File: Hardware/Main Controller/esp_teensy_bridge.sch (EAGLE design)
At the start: 9 parts, among them IC1 BQ79600PWRQ1

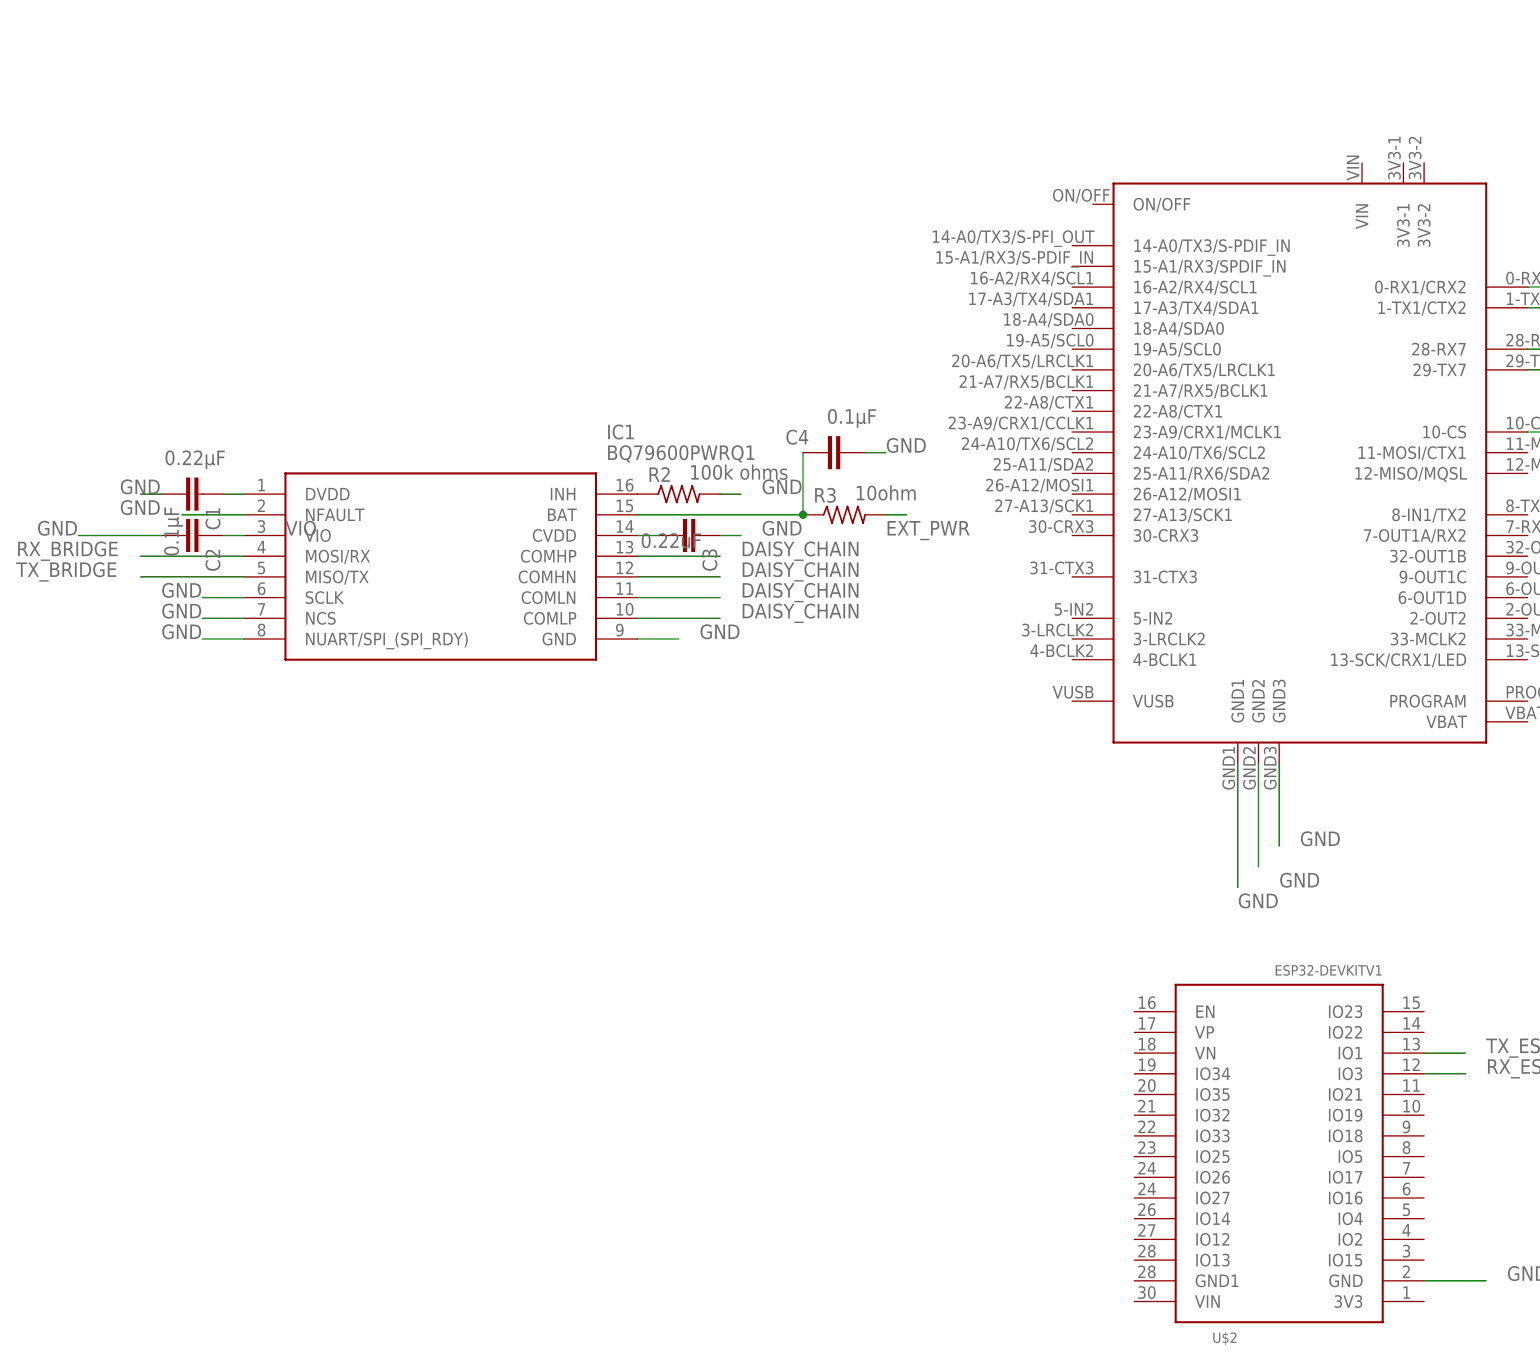
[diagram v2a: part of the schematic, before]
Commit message: Update esp_teensy_bridge.sch
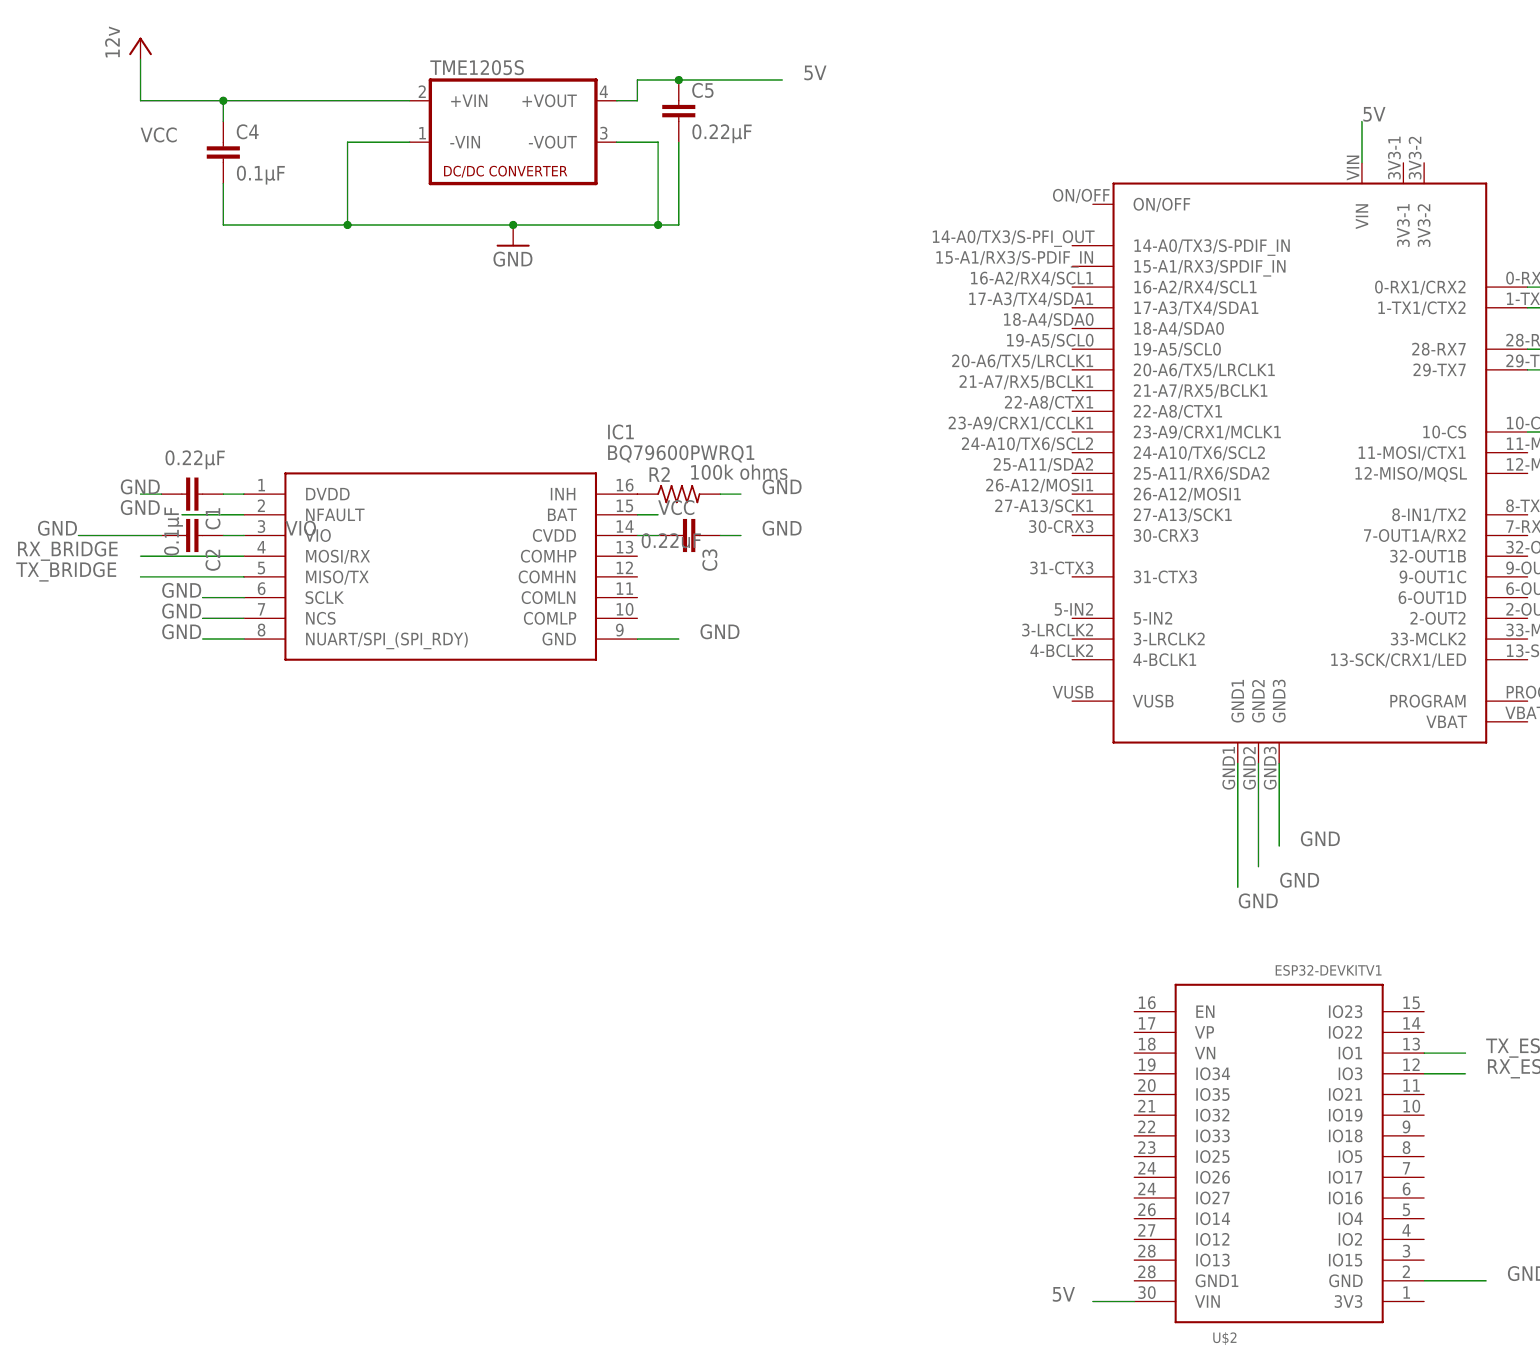
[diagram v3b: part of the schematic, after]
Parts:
- removed R3: 10ohm, rcl:R-US_0204/7
- added C5: 0.22μF, capacitor-wima:C2,5-3
- added TME1205S: (no value), dc-dc-converter:NME
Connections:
- removed net DAISY_CHAIN: IC1.COMHN, IC1.COMHP, IC1.COMLN, IC1.COMLP
- removed net EXT_PWR: R3.2
- removed net N$5: C4.2, IC1.BAT, R3.1
- new net 5V: C5.1, TME1205S.+VOUT, U$1.VIN, U$2.VIN
- new net VCC: C4.1, IC1.BAT, TME1205S.+VIN
- net GND: now also C4.2, C5.2, TME1205S.-VIN, TME1205S.-VOUT; no longer C4.1
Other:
- moved on the sheet: C4
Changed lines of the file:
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@@
 <part name="C3" library="capacitor-wima" library_urn="urn:adsk.eagle:library:116" deviceset="C" device="2.5/2" package3d_urn="urn:adsk.eagle:package:5415/1" value="0.22uF"/>
 <part name="R2" library="rcl" library_urn="urn:adsk.eagle:library:334" deviceset="R-US_" device="0204/7" package3d_urn="urn:adsk.eagle:package:23498/2" value="100k ohms"/>
-<part name="R3" library="rcl" library_urn="urn:adsk.eagle:library:334" deviceset="R-US_" device="0204/7" package3d_urn="urn:adsk.eagle:package:23498/2" value="10ohm"/>
+<part name="TME1205S" library="dc-dc-converter" library_urn="urn:adsk.eagle:library:208" deviceset="NME" device="" package3d_urn="urn:adsk.eagle:package:12313/1"/>
+<part name="GND1" library="supply1" library_urn="urn:adsk.eagle:library:371" deviceset="GND" device=""/>
+<part name="C5" library="capacitor-wima" library_urn="urn:adsk.eagle:library:116" deviceset="C" device="2,5-3" package3d_urn="urn:adsk.eagle:package:5436/1" value="0.22μF"/>
+<part name="P+1" library="supply1" library_urn="urn:adsk.eagle:library:371" deviceset="VCC" device="" value="12v"/>
 <part name="C4" library="capacitor-wima" library_urn="urn:adsk.eagle:library:116" deviceset="C" device="2,5-3" package3d_urn="urn:adsk.eagle:package:5436/1" value="0.1μF"/>
 </parts>
@@
 <attribute name="VALUE" x="-8.89" y="67.818" size="1.778" layer="96"/>
 </instance>
-<instance part="R3" gate="G$1" x="10.16" y="63.5" smashed="yes">
-<attribute name="NAME" x="6.35" y="64.9986" size="1.778" layer="95"/>
-<attribute name="VALUE" x="11.43" y="65.278" size="1.778" layer="96"/>
-</instance>
-<instance part="C4" gate="G$1" x="10.16" y="71.12" smashed="yes" rot="R270">
-<attribute name="NAME" x="2.921" y="72.136" size="1.778" layer="95"/>
-<attribute name="VALUE" x="8.001" y="74.676" size="1.778" layer="96"/>
+<instance part="TME1205S" gate="G$1" x="-30.48" y="111.76" smashed="yes">
+<attribute name="NAME" x="-40.64" y="117.475" size="1.778" layer="95"/>
+<attribute name="VALUE" x="-40.64" y="101.6" size="1.778" layer="96"/>
+</instance>
+<instance part="GND1" gate="1" x="-30.48" y="96.52" smashed="yes">
+<attribute name="VALUE" x="-33.02" y="93.98" size="1.778" layer="96"/>
+</instance>
+<instance part="C5" gate="G$1" x="-10.16" y="114.3" smashed="yes">
+<attribute name="NAME" x="-8.636" y="114.681" size="1.778" layer="95"/>
+<attribute name="VALUE" x="-8.636" y="109.601" size="1.778" layer="96"/>
+</instance>
+<instance part="P+1" gate="VCC" x="-76.2" y="121.92" smashed="yes">
+<attribute name="VALUE" x="-78.74" y="119.38" size="1.778" layer="96" rot="R90"/>
+</instance>
+<instance part="C4" gate="G$1" x="-66.04" y="109.22" smashed="yes">
+<attribute name="NAME" x="-64.516" y="109.601" size="1.778" layer="95"/>
+<attribute name="VALUE" x="-64.516" y="104.521" size="1.778" layer="96"/>
 </instance>
 </instances>
@@
 </busses>
 <nets>
-<net name="DAISY_CHAIN" class="0">
-<segment>
-<pinref part="IC1" gate="G$1" pin="COMHP"/>
-<wire x1="-15.24" y1="58.42" x2="-5.08" y2="58.42" width="0.1524" layer="91"/>
-<label x="-2.54" y="58.42" size="1.778" layer="95"/>
-</segment>
-<segment>
-<pinref part="IC1" gate="G$1" pin="COMHN"/>
-<wire x1="-15.24" y1="55.88" x2="-5.08" y2="55.88" width="0.1524" layer="91"/>
-<label x="-2.54" y="55.88" size="1.778" layer="95"/>
-</segment>
-<segment>
-<pinref part="IC1" gate="G$1" pin="COMLN"/>
-<wire x1="-15.24" y1="53.34" x2="-5.08" y2="53.34" width="0.1524" layer="91"/>
-<label x="-2.54" y="53.34" size="1.778" layer="95"/>
-</segment>
-<segment>
-<pinref part="IC1" gate="G$1" pin="COMLP"/>
-<wire x1="-15.24" y1="50.8" x2="-5.08" y2="50.8" width="0.1524" layer="91"/>
-<label x="-2.54" y="50.8" size="1.778" layer="95"/>
-</segment>
-</net>
 <net name="GND" class="0">
 <segment>
@@
 </segment>
 <segment>
-<pinref part="C4" gate="G$1" pin="1"/>
-<wire x1="12.7" y1="71.12" x2="15.24" y2="71.12" width="0.1524" layer="91"/>
-<label x="15.24" y="71.12" size="1.778" layer="95"/>
-</segment>
-<segment>
 <pinref part="IC1" gate="G$1" pin="SCLK"/>
 <wire x1="-63.5" y1="53.34" x2="-68.58" y2="53.34" width="0.1524" layer="91"/>
@@
 <wire x1="-63.5" y1="50.8" x2="-68.58" y2="50.8" width="0.1524" layer="91"/>
 <label x="-73.66" y="50.8" size="1.778" layer="95"/>
+</segment>
+<segment>
+<pinref part="TME1205S" gate="G$1" pin="-VIN"/>
+<wire x1="-50.8" y1="109.22" x2="-43.18" y2="109.22" width="0.1524" layer="91"/>
+<wire x1="-50.8" y1="109.22" x2="-50.8" y2="99.06" width="0.1524" layer="91"/>
+<wire x1="-50.8" y1="99.06" x2="-30.48" y2="99.06" width="0.1524" layer="91"/>
+<wire x1="-30.48" y1="99.06" x2="-12.7" y2="99.06" width="0.1524" layer="91"/>
+<pinref part="GND1" gate="1" pin="GND"/>
+<junction x="-30.48" y="99.06"/>
+<pinref part="C4" gate="G$1" pin="2"/>
+<wire x1="-66.04" y1="104.14" x2="-66.04" y2="99.06" width="0.1524" layer="91"/>
+<wire x1="-66.04" y1="99.06" x2="-50.8" y2="99.06" width="0.1524" layer="91"/>
+<junction x="-50.8" y="99.06"/>
+<pinref part="TME1205S" gate="G$1" pin="-VOUT"/>
+<wire x1="-17.78" y1="109.22" x2="-12.7" y2="109.22" width="0.1524" layer="91"/>
+<wire x1="-12.7" y1="109.22" x2="-12.7" y2="99.06" width="0.1524" layer="91"/>
+<wire x1="-12.7" y1="99.06" x2="-10.16" y2="99.06" width="0.1524" layer="91"/>
+<junction x="-12.7" y="99.06"/>
+<pinref part="C5" gate="G$1" pin="2"/>
+<wire x1="-10.16" y1="99.06" x2="-10.16" y2="109.22" width="0.1524" layer="91"/>
 </segment>
 </net>
@@
 </segment>
 </net>
-<net name="N$5" class="0">
-<segment>
-<pinref part="IC1" gate="G$1" pin="BAT"/>
-<wire x1="-15.24" y1="63.5" x2="5.08" y2="63.5" width="0.1524" layer="91"/>
-<pinref part="C4" gate="G$1" pin="2"/>
-<wire x1="5.08" y1="71.12" x2="5.08" y2="63.5" width="0.1524" layer="91"/>
-<pinref part="R3" gate="G$1" pin="1"/>
-<junction x="5.08" y="63.5"/>
-</segment>
-</net>
-<net name="EXT_PWR" class="0">
-<segment>
-<pinref part="R3" gate="G$1" pin="2"/>
-<wire x1="15.24" y1="63.5" x2="17.78" y2="63.5" width="0.1524" layer="91"/>
-<label x="15.24" y="60.96" size="1.778" layer="95"/>
-</segment>
-</net>
 <net name="TX_ESP" class="0">
 <segment>
@@
 </segment>
 </net>
+<net name="5V" class="0">
+<segment>
+<pinref part="U$1" gate="G$1" pin="VIN"/>
+<wire x1="73.66" y1="106.68" x2="73.66" y2="111.76" width="0.1524" layer="91"/>
+<label x="73.66" y="111.76" size="1.778" layer="95"/>
+</segment>
+<segment>
+<pinref part="U$2" gate="G$1" pin="VIN"/>
+<wire x1="45.72" y1="-33.02" x2="40.64" y2="-33.02" width="0.1524" layer="91"/>
+<label x="35.56" y="-33.02" size="1.778" layer="95"/>
+</segment>
+<segment>
+<pinref part="TME1205S" gate="G$1" pin="+VOUT"/>
+<wire x1="-17.78" y1="114.3" x2="-15.24" y2="114.3" width="0.1524" layer="91"/>
+<wire x1="-15.24" y1="114.3" x2="-15.24" y2="116.84" width="0.1524" layer="91"/>
+<pinref part="C5" gate="G$1" pin="1"/>
+<wire x1="-15.24" y1="116.84" x2="-10.16" y2="116.84" width="0.1524" layer="91"/>
+<wire x1="-10.16" y1="116.84" x2="2.54" y2="116.84" width="0.1524" layer="91"/>
+<junction x="-10.16" y="116.84"/>
+<label x="5.08" y="116.84" size="1.778" layer="95"/>
+</segment>
+</net>
+<net name="VCC" class="0">
+<segment>
+<pinref part="P+1" gate="VCC" pin="VCC"/>
+<wire x1="-76.2" y1="119.38" x2="-76.2" y2="114.3" width="0.1524" layer="91"/>
+<pinref part="TME1205S" gate="G$1" pin="+VIN"/>
+<wire x1="-76.2" y1="114.3" x2="-66.04" y2="114.3" width="0.1524" layer="91"/>
+<pinref part="C4" gate="G$1" pin="1"/>
+<wire x1="-66.04" y1="114.3" x2="-43.18" y2="114.3" width="0.1524" layer="91"/>
+<wire x1="-66.04" y1="111.76" x2="-66.04" y2="114.3" width="0.1524" layer="91"/>
+<junction x="-66.04" y="114.3"/>
+<label x="-76.2" y="109.22" size="1.778" layer="95"/>
+</segment>
+<segment>
+<pinref part="IC1" gate="G$1" pin="BAT"/>
+<wire x1="-15.24" y1="63.5" x2="-12.7" y2="63.5" width="0.1524" layer="91"/>
+<label x="-12.7" y="63.5" size="1.778" layer="95"/>
+</segment>
+</net>
